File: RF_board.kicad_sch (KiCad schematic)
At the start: 2 parts, among them J1 Conn_Coaxial, U1 SPF5189Z

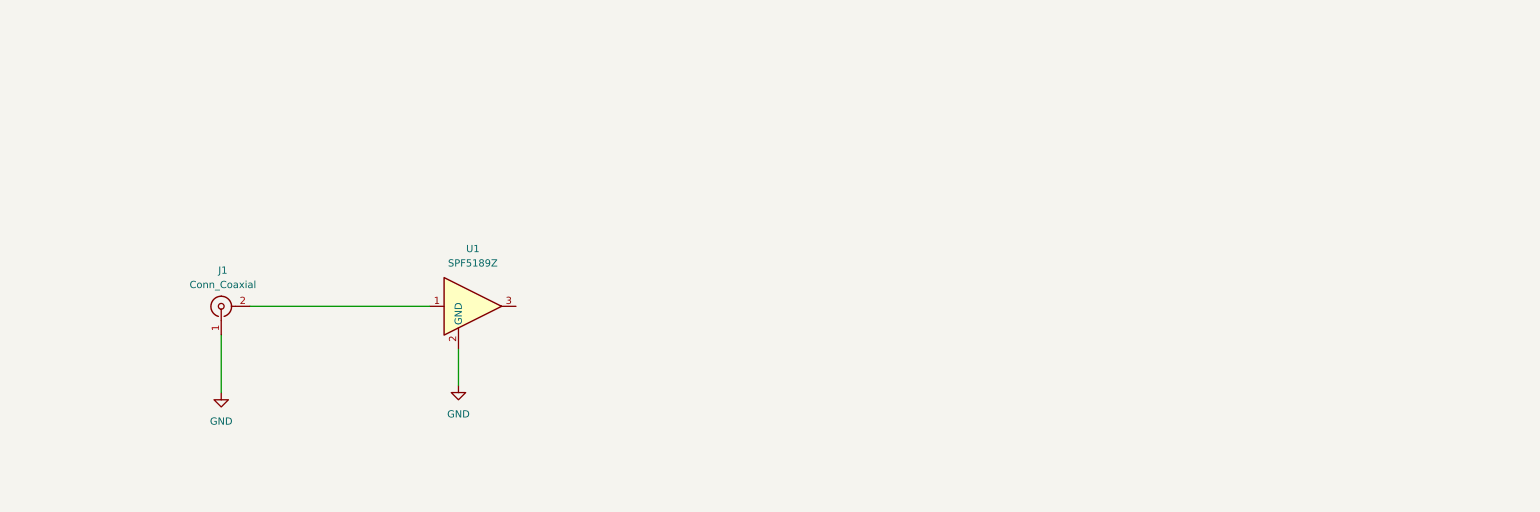
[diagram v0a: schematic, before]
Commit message: added ground stitching vias to SMA connector
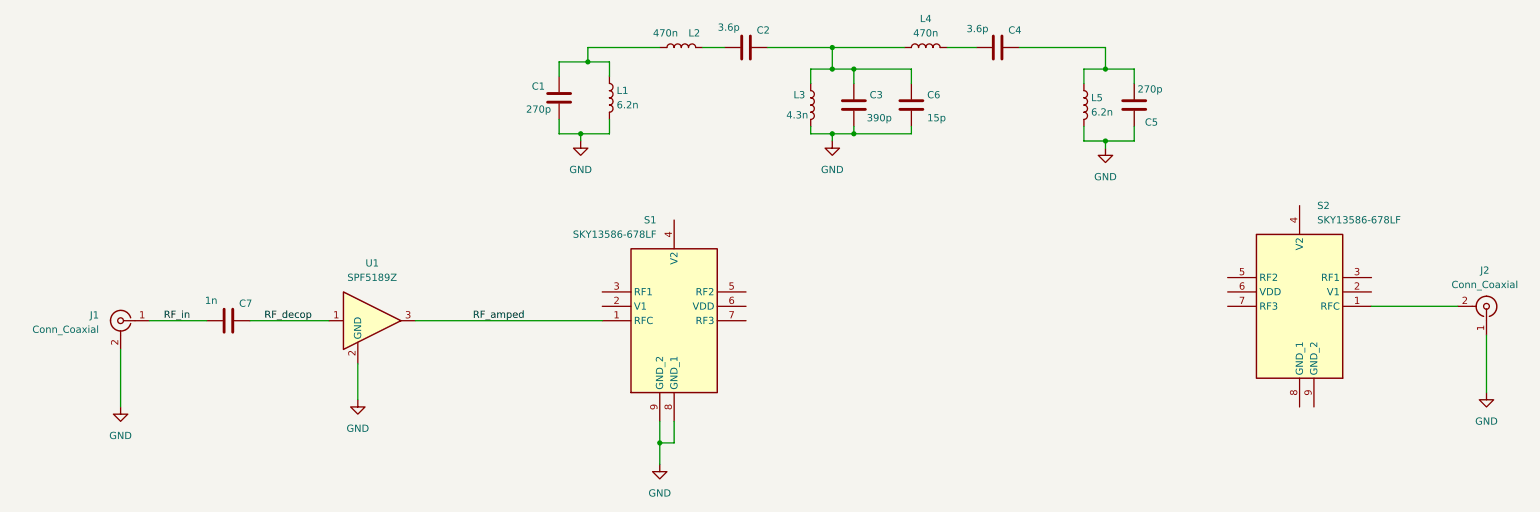
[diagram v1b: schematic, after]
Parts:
- added C1, C5: 270p, symbol Device:C
- added C2, C4: 3.6p, symbol Device:C
- added C3: 390p, symbol Device:C
- added C6: 15p, symbol Device:C
- added C7: 1n, Capacitor_SMD:C_0603_1608Metric, symbol Device:C
- added J2: Conn_Coaxial, Connector_Coaxial:SMA_Amphenol_132289_EdgeMount, symbol Connector:Conn_Coaxial
- added L1: 6.2n, Inductor_SMD:L_0603_1608Metric, symbol Device:L
- added L2, L4: 470n, symbol Device:L
- added L3: 4.3n, symbol Device:L
- added L5: 6.2n, symbol Device:L
- added S1, S2: SKY13586-678LF, RF_board_footprints:SKY13586678LF, symbol SKY13586-678LF:SKY13586-678LF
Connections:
- net GND: now also J1.2 (Ext), C1.2, C3.2, C5.2, C6.2, J2.1 (In), L1.2, L3.2, L5.2, S1.8 (GND_1), S1.9 (GND_2); no longer J1.1 (In)
- net RF_decop: now reaches U1.1
- net RF_decop: now also C7.2; no longer J1.2 (Ext)
- net RF_amped: now reaches U1.3
- net RF_amped: now also S1.1 (RFC)
- new net: C2.1, L2.2
- new net: C2.2, C3.1, C6.1, L3.1, L4.1
- new net: C4.1, L4.2
- new net: C1.1, L1.1, L2.1
- new net: C4.2, C5.1, L5.1
- new net: J2.2 (Ext), S2.1 (RFC)
- new net RF_in: C7.1, J1.1 (In)
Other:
- moved on the sheet: J1, U1
